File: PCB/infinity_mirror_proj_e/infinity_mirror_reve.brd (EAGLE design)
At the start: 55 x 37 mm, 35 parts, among them J1 POWER_JACKPTH_BREAD, J2 CAP, J3 SERIAL, Q1 800mA/40V, Q2 800mA/40V, Q3 BSS138, U1 3.3LDO

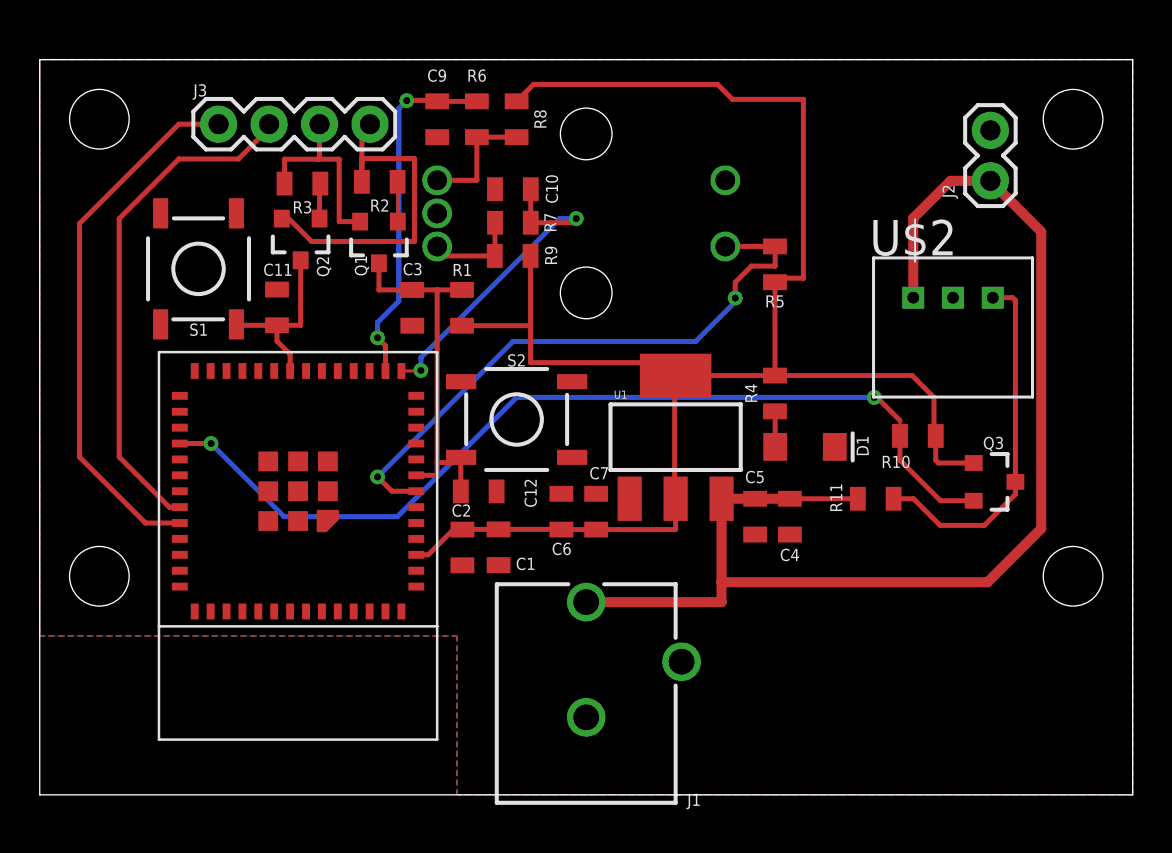
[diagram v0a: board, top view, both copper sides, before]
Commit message: encoder footprint fix
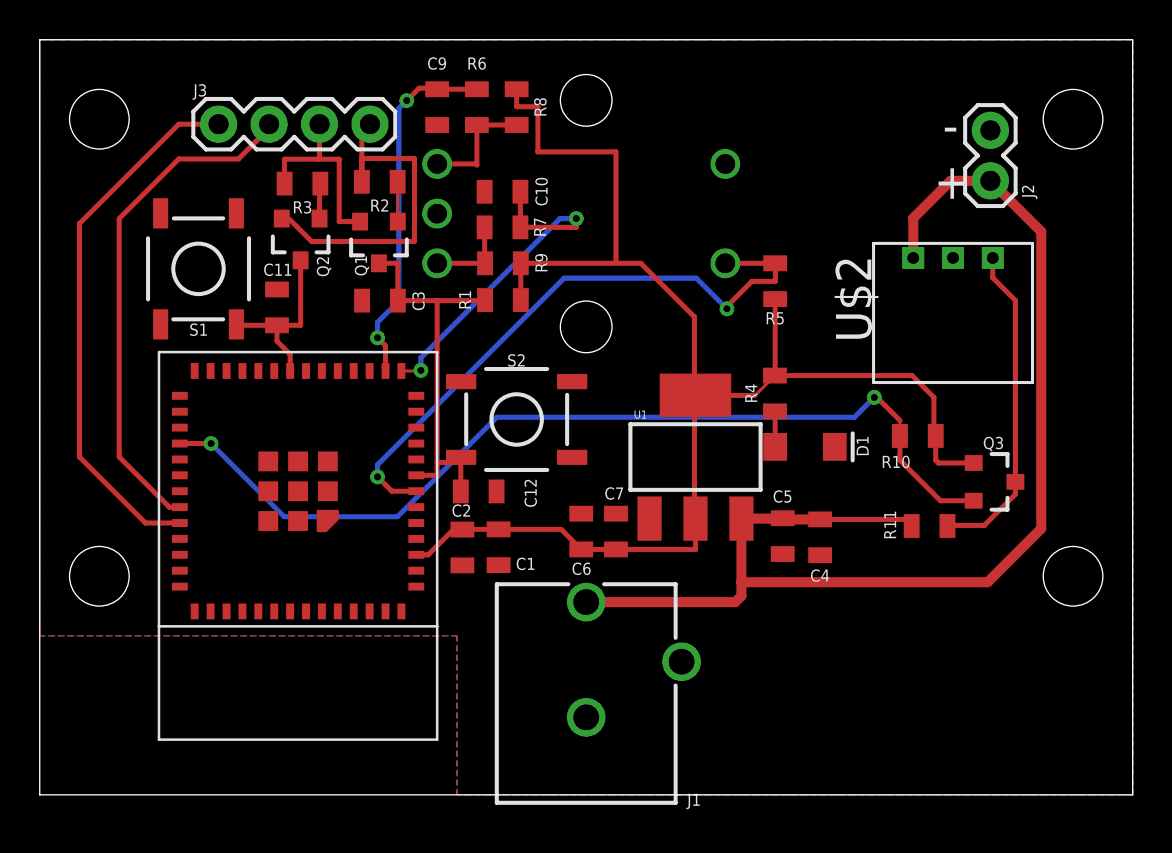
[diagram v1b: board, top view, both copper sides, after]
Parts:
- J2: value CAP -> LED_CAP
- moved R11 3.04 mm to (44.8, 13.5)
- moved R1 2.10 mm to (23.3, 24.9), turned to 0 degrees
- moved U$2 2.00 mm to (46.0, 27.0)
- moved C4 1.84 mm to (39.3, 13.0)
- moved C5 1.70 mm to (37.4, 13.0)
- moved C3 1.67 mm to (17.1, 24.9), turned to 180 degrees
- moved C6 1.41 mm to (27.2, 13.2)
- moved C7 1.41 mm to (29.0, 13.2)
- moved U1 1.41 mm to (33.0, 17.0)
- moved R5 0.85 mm to (37.0, 25.9)
- moved R9 0.61 mm to (23.3, 26.8)
- moved C9 0.61 mm to (20.0, 34.6)
- moved R6 0.61 mm to (22.0, 34.6)
- moved R8 0.61 mm to (24.0, 34.6)
- moved R7 0.57 mm to (23.3, 28.6)
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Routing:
- net VCC_2: track 86.7 -> 74.1 mm
- net LED_DATA: track 18.3 -> 16.5 mm
- net VCC_1: track 63.3 -> 62.0 mm
- net ESP_RST: track 18.9 -> 20.1 mm
- net ENC_A: track 16.4 -> 17.4 mm
- net BUTTON: track 30.7 -> 31.5 mm
- net N$3: track 4.77 -> 4.23 mm
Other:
- board size 55 x 37 mm -> 55 x 38 mm
- board text added: "+"
- board text added: "-"
